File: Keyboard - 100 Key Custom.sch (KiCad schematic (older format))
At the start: 223 parts, among them J1 TYPE-C-31-M12_13, K1 Esc, K10 A, K100 P_+, K101 P_Enter_200v, K11 Z, K12 Win_L_125, K13 F2, K14 2(@), K15 W, K16 S, K17 X, K18 Alt_L_125, K19 F3, K2 `(~~), K20 3(#), K21 E, K22 D, K23 C, K24 F4, K25 4($), K26 R, K27 F, K28 V, K29 F5, K3 Tab_150, K30 5(%), K31 T, K32 G, K33 B, K34 Space_625, K35 F6, K36 6(^), K37 Y, K38 H, K39 N, K4 Caps_Lock_175, K40 F7, K41 7(&), K42 U, K43 J, K44 M, K45 F8, K46 8(*), K47 I, K48 K, K49 ,(<), K5 Shift_L_225, K50 F9, K51 9((), K52 O, K53 L, K54 .(>), K55 Alt_R, K56 F10, K57 0()), K58 P, K59 ;(:), K6 Ctrl_L_125, K60 /(?), K61 Function, K62 F11, K63 -(_), K64 [({), K65 '(\"), K66 Ctrl_R, K67 F12, K68 =(+), K69 ](}), K7 F1, K70 Shift_R_175, K71 Left, K72 Print_Screen, K73 Backspace_200, K74 \\(|)_150, K75 Enter_225, K76 Up, K77 Down, K78 Delete, K79 Insert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

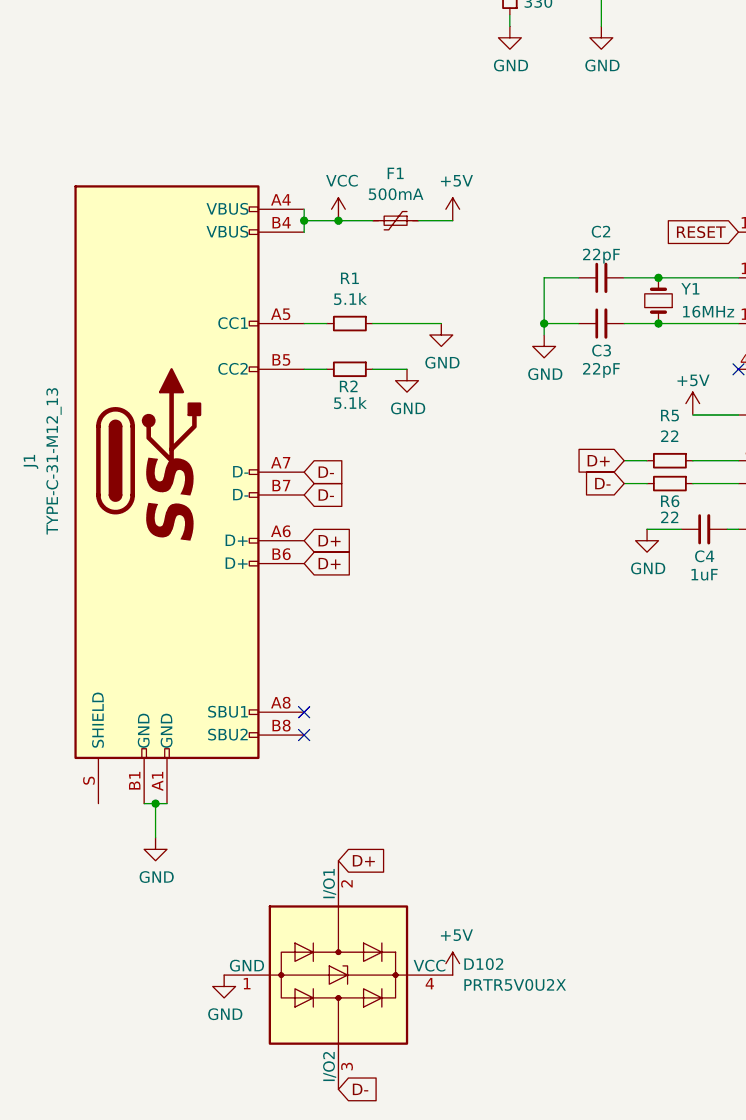
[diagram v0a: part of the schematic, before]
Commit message: Updated USB-C connector to interface with Daughterboard instead
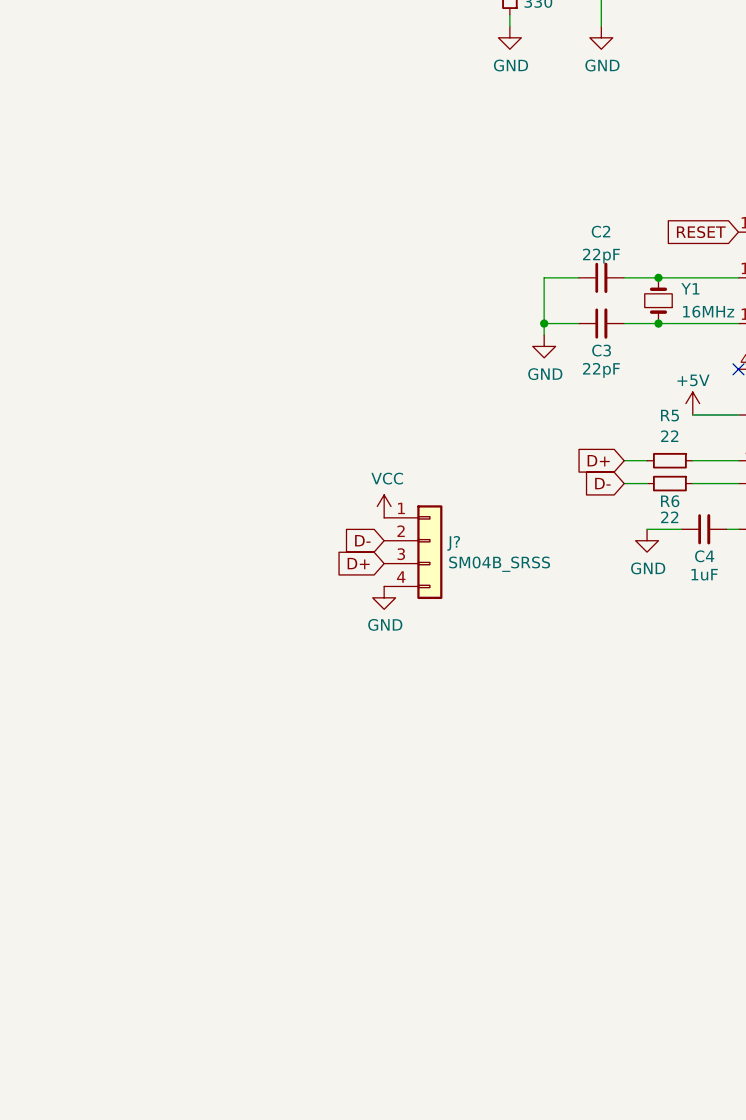
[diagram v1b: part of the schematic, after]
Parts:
- removed D102: PRTR5V0U2X, Package_TO_SOT_SMD:SOT-143, symbol Power_Protection:PRTR5V0U2X
- removed F1: 500mA, Fuse:Fuse_0805_2012Metric_Pad1.15x1.40mm_HandSolder, symbol Device:Polyfuse_Small
- removed J1: TYPE-C-31-M12_13, acheronLibrary Connectors:TYPE-C-31-M-12, symbol acheronSymbols:TYPE-C-31-M12_13
- removed R1, R2: 5.1k, Capacitor_SMD:C_1206_3216Metric_Pad1.42x1.75mm_HandSolder, symbol Device:R_Small
- added J?: SM04B_SRSS, symbol Connector_Generic:Conn_01x04
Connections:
- net D+: now also J?.3 (Pin_3)
- net D-: now also J?.2 (Pin_2)
- net GND: now also J?.4 (Pin_4)
- net VCC: now also J?.1 (Pin_1)
- no-connect marks 3 -> 1

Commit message: Started tracing
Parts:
- J1: renamed from J?; footprint (none) -> acheronLibrary Connectors:SM04B-SRSS
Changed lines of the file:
@@
 col18
 $Comp
-L power:VCC #PWR?
+L power:VCC #PWR0113
 U 1 1 5E9BC47F
 P 2500 4250
-F 0 "#PWR?" H 2500 4100 50  0001 C CNN
+F 0 "#PWR0113" H 2500 4100 50  0001 C CNN
 F 1 "VCC" H 2515 4420 50  0000 C CNN
 F 2 "" H 2500 4250 50  0001 C CNN
@@
 $EndComp
 $Comp
-L power:GND #PWR?
+L power:GND #PWR0112
 U 1 1 5E9C03BF
 P 2500 4550
-F 0 "#PWR?" H 2500 4300 50  0001 C CNN
+F 0 "#PWR0112" H 2500 4300 50  0001 C CNN
 F 1 "GND" H 2505 4380 50  0000 C CNN
 F 2 "" H 2500 4550 50  0001 C CNN
@@
 $EndComp
 $Comp
-L Connector_Generic:Conn_01x04 J?
+L Connector_Generic:Conn_01x04 J1
 U 1 1 5E9BA46C
 P 2700 4350
-F 0 "J?" H 2780 4343 50  0000 L CNN
+F 0 "J1" H 2780 4343 50  0000 L CNN
 F 1 "SM04B_SRSS" H 2780 4253 50  0000 L CNN
-F 2 "" H 2700 4350 50  0001 C CNN
+F 2 "acheronLibrary Connectors:SM04B-SRSS" H 2700 4350 50  0001 C CNN
 F 3 "~" H 2700 4350 50  0001 C CNN
 	1    2700 4350

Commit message: Placed components roughly and traced rows and columns.
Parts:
- U1: footprint Package_QFP:TQFP-44_10x10mm_P0.8mm -> acheronLibrary Components:QFN-44-1EP_7x7mm_P0.5mm_EP5.2x5.2mm
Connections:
- net VCC is gone; now on net +5V: J1.1 (Pin_1)
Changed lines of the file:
@@
 col18
 $Comp
-L power:VCC #PWR0113
-U 1 1 5E9BC47F
+L power:+5V #PWR?
+U 1 1 5E9DDDC6
 P 2500 4250
-F 0 "#PWR0113" H 2500 4100 50  0001 C CNN
-F 1 "VCC" H 2515 4420 50  0000 C CNN
+F 0 "#PWR?" H 2500 4100 50  0001 C CNN
+F 1 "+5V" H 2515 4420 50  0000 C CNN
 F 2 "" H 2500 4250 50  0001 C CNN
 F 3 "" H 2500 4250 50  0001 C CNN
@@
 F 0 "U1" H 4400 4300 50  0000 C CNN
 F 1 "ATmega32U4-AU" H 4500 4200 50  0000 C CNN
-F 2 "Package_QFP:TQFP-44_10x10mm_P0.8mm" H 4650 4500 50  0001 C CIN
+F 2 "acheronLibrary Components:QFN-44-1EP_7x7mm_P0.5mm_EP5.2x5.2mm" H 4650 4500 50  0001 C CIN
 F 3 "http://ww1.microchip.com/downloads/en/DeviceDoc/Atmel-7766-8-bit-AVR-ATmega16U4-32U4_Datasheet.pdf" H 4650 4500 50  0001 C CNN
 	1    4650 4500

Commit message: Added traces besides rows/columns
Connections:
- net row4: now also U1.1 (PE6)
- net row5: now also U1.41 (PF0)
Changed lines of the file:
@@
 Text GLabel 4050 3000 0    50   Input ~ 0
 RESET
+Text GLabel 5250 5200 2    50   Input ~ 0
+row4
+Text GLabel 5250 5400 2    50   Input ~ 0
+row5
 Text GLabel 7750 1650 0    50   Input ~ 0
 row0
@@
 col18
 $Comp
-L power:+5V #PWR?
+L power:+5V #PWR0113
 U 1 1 5E9DDDC6
 P 2500 4250
-F 0 "#PWR?" H 2500 4100 50  0001 C CNN
+F 0 "#PWR0113" H 2500 4100 50  0001 C CNN
 F 1 "+5V" H 2515 4420 50  0000 C CNN
 F 2 "" H 2500 4250 50  0001 C CNN

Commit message: Replaced MCU with hand-solder model and retraced.
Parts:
- U1: footprint acheronLibrary Components:QFN-44-1EP_7x7mm_P0.5mm_EP5.2x5.2mm -> acheronLibrary Components:TQPF-44_10x10mm_P0.8mm
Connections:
- net row4: no longer U1.1 (PE6)
- net row5: no longer U1.41 (PF0)
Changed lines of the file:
@@
 Text GLabel 4050 3000 0    50   Input ~ 0
 RESET
-Text GLabel 5250 5200 2    50   Input ~ 0
-row4
-Text GLabel 5250 5400 2    50   Input ~ 0
-row5
 Text GLabel 7750 1650 0    50   Input ~ 0
 row0
@@
 F 0 "U1" H 4400 4300 50  0000 C CNN
 F 1 "ATmega32U4-AU" H 4500 4200 50  0000 C CNN
-F 2 "acheronLibrary Components:QFN-44-1EP_7x7mm_P0.5mm_EP5.2x5.2mm" H 4650 4500 50  0001 C CIN
+F 2 "acheronLibrary Components:TQPF-44_10x10mm_P0.8mm" H 4650 4500 50  0001 C CIN
 F 3 "http://ww1.microchip.com/downloads/en/DeviceDoc/Atmel-7766-8-bit-AVR-ATmega16U4-32U4_Datasheet.pdf" H 4650 4500 50  0001 C CNN
 	1    4650 4500

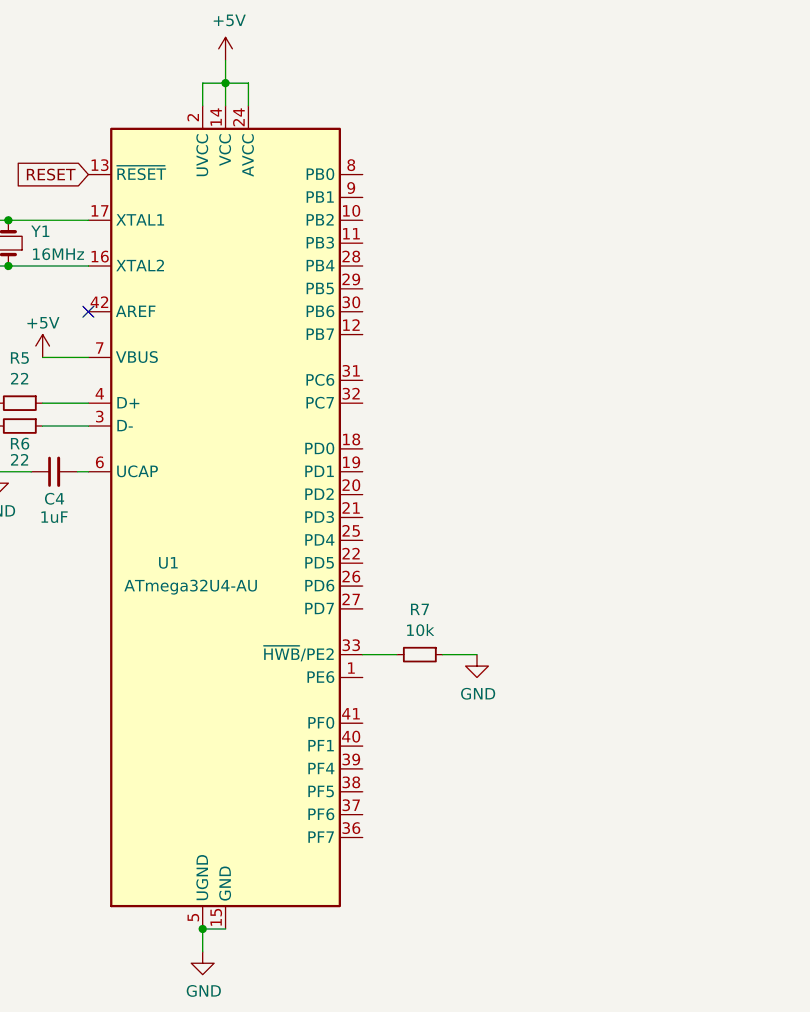
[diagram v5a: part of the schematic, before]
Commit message: Finished Running Traces
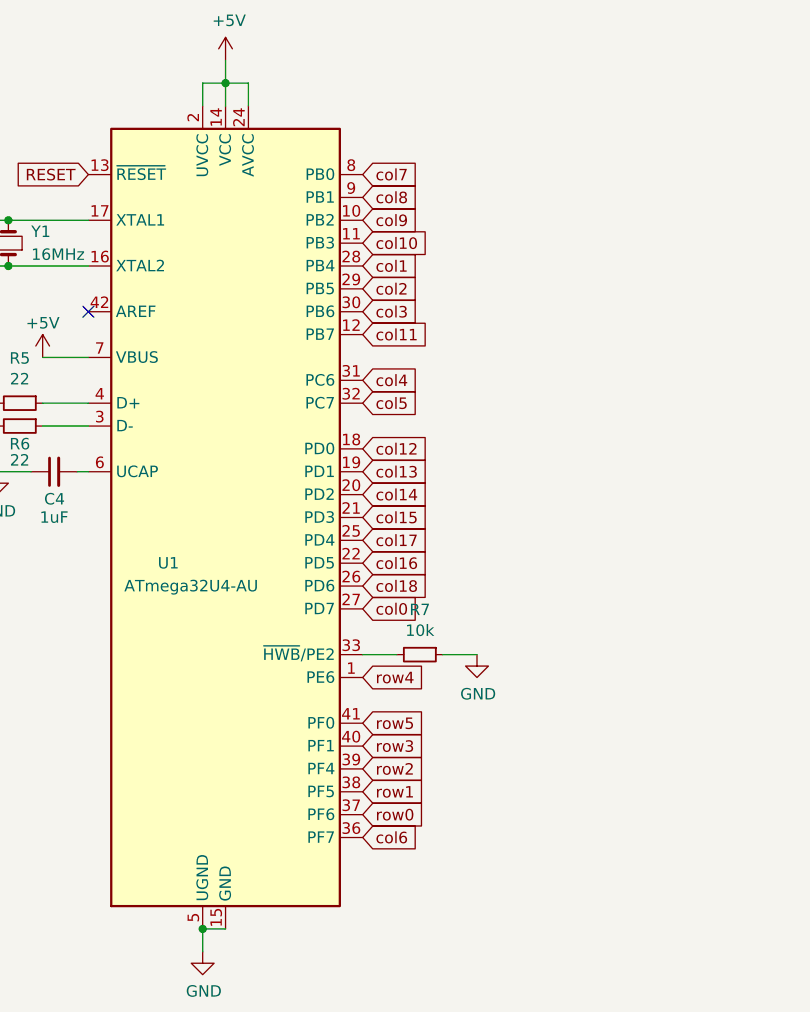
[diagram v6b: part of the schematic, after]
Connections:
- net col0: now also U1.27 (PD7)
- net col1: now also U1.28 (PB4)
- net col10: now also U1.11 (PB3)
- net col11: now also U1.12 (PB7)
- net col12: now also U1.18 (PD0)
- net col13: now also U1.19 (PD1)
- net col14: now also U1.20 (PD2)
- net col15: now also U1.21 (PD3)
- net col16: now also U1.22 (PD5)
- net col17: now also U1.25 (PD4)
- net col18: now also U1.26 (PD6)
- net col2: now also U1.29 (PB5)
- net col3: now also U1.30 (PB6)
- net col4: now also U1.31 (PC6)
- net col5: now also U1.32 (PC7)
- net col6: now also U1.36 (PF7)
- net col7: now also U1.8 (PB0)
- net col8: now also U1.9 (PB1)
- net col9: now also U1.10 (PB2)
- net row0: now also U1.37 (PF6)
- net row1: now also U1.38 (PF5)
- net row2: now also U1.39 (PF4)
- net row3: now also U1.40 (PF1)
- net row4: now also U1.1 (PE6)
- net row5: now also U1.41 (PF0)
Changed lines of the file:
@@
 Text GLabel 4050 3000 0    50   Input ~ 0
 RESET
+Text GLabel 5250 3000 2    50   Input ~ 0
+col7
+Text GLabel 5250 3100 2    50   Input ~ 0
+col8
+Text GLabel 5250 3200 2    50   Input ~ 0
+col9
+Text GLabel 5250 3300 2    50   Input ~ 0
+col10
+Text GLabel 5250 3400 2    50   Input ~ 0
+col1
+Text GLabel 5250 3500 2    50   Input ~ 0
+col2
+Text GLabel 5250 3600 2    50   Input ~ 0
+col3
+Text GLabel 5250 3700 2    50   Input ~ 0
+col11
+Text GLabel 5250 3900 2    50   Input ~ 0
+col4
+Text GLabel 5250 4000 2    50   Input ~ 0
+col5
+Text GLabel 5250 4200 2    50   Input ~ 0
+col12
+Text GLabel 5250 4300 2    50   Input ~ 0
+col13
+Text GLabel 5250 4400 2    50   Input ~ 0
+col14
+Text GLabel 5250 4500 2    50   Input ~ 0
+col15
+Text GLabel 5250 4600 2    50   Input ~ 0
+col17
+Text GLabel 5250 4700 2    50   Input ~ 0
+col16
+Text GLabel 5250 4800 2    50   Input ~ 0
+col18
+Text GLabel 5250 4900 2    50   Input ~ 0
+col0
+Text GLabel 5250 5200 2    50   Input ~ 0
+row4
+Text GLabel 5250 5400 2    50   Input ~ 0
+row5
+Text GLabel 5250 5500 2    50   Input ~ 0
+row3
+Text GLabel 5250 5600 2    50   Input ~ 0
+row2
+Text GLabel 5250 5700 2    50   Input ~ 0
+row1
+Text GLabel 5250 5800 2    50   Input ~ 0
+row0
+Text GLabel 5250 5900 2    50   Input ~ 0
+col6
 Text GLabel 7750 1650 0    50   Input ~ 0
 row0
